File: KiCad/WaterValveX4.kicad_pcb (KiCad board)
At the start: 2 copper layers, 63.2 x 39.1 mm, 51 parts, among them J1 Conn_01x04_Male, J2 Barrel_Jack, J3 Conn_01x03_Male, J4 Conn_01x01_Male, J5 Conn_01x04_Male, J6 Screw_Terminal_01x03, J7 Screw_Terminal_01x03, J8 Screw_Terminal_01x03, J9 Screw_Terminal_01x02, Q1 IRLML2502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

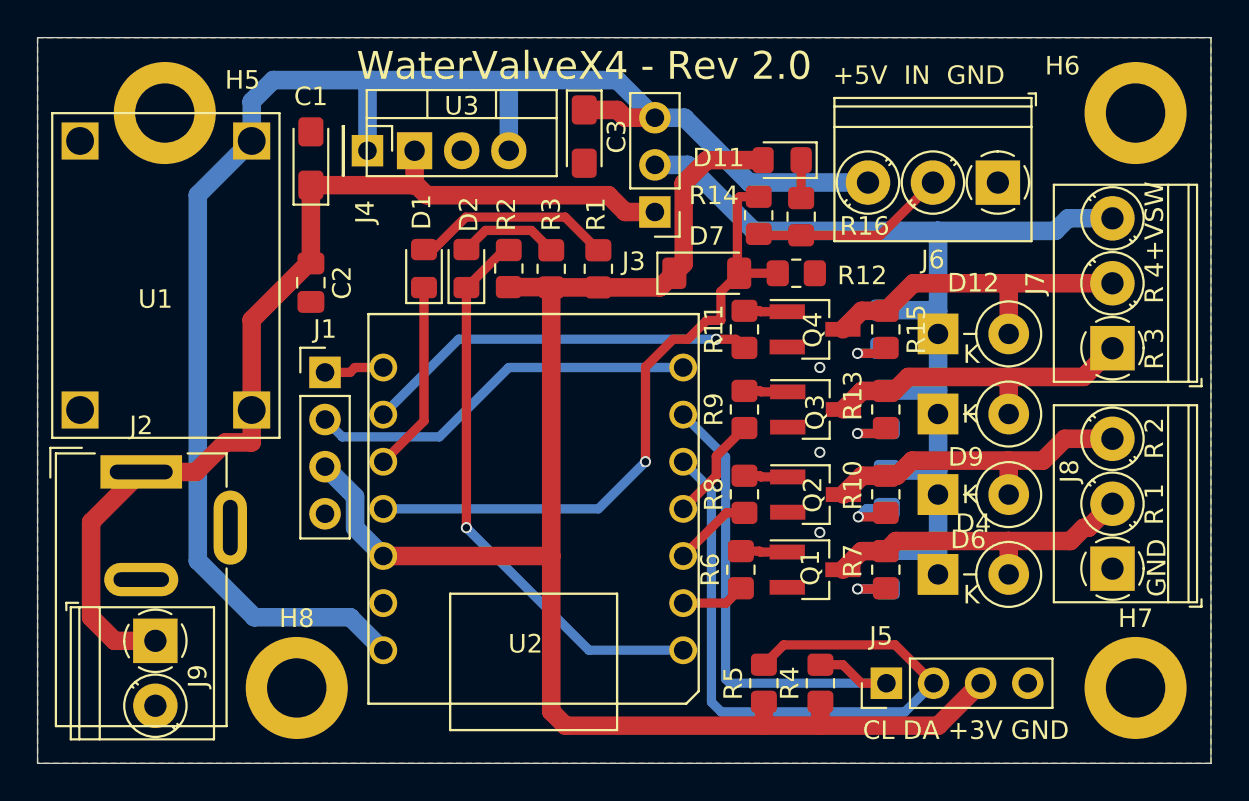
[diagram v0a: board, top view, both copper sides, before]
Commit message: Version 2.0.1 - pulled up / level shifted flow input
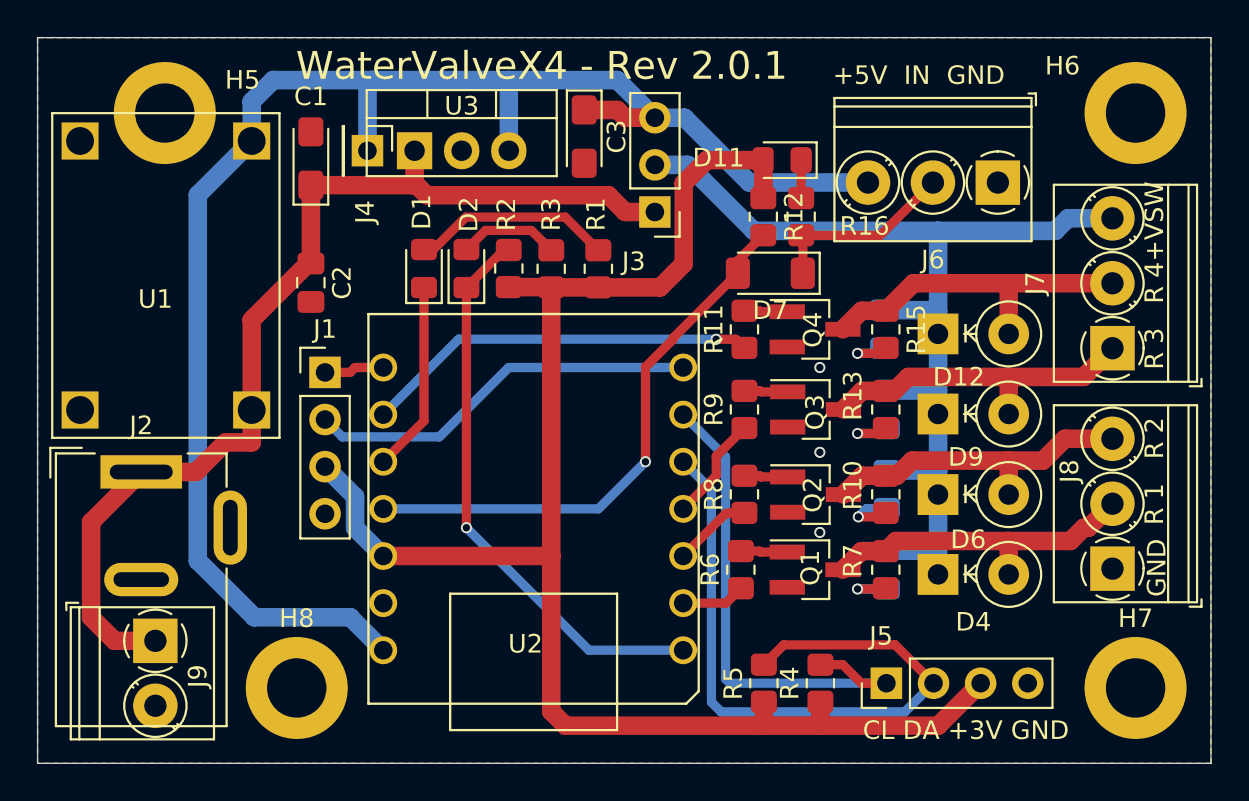
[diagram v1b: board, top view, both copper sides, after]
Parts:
- removed R14: 2.2k, Resistor_SMD:R_0805_2012Metric_Pad1.20x1.40mm_HandSolder
- R10, R13, R15, R7: value 330 -> 1k
- R12: value 3.3k -> 10k
- moved R12 3.53 mm to (175.0, 94.4), turned to -90 degrees
- moved D7 3.43 mm to (175.4, 97.4), turned to 180 degrees
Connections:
- D7 pad 1: +3V3 -> Net-(D7-K)
- J6 pad 2: Net-(J6-Pin_2) -> Net-(D7-K)
- R12 pad 1: /GPIO10 -> +3V3
- R12 pad 2: GND -> /GPIO10
- R16 pad 1: Net-(J6-Pin_2) -> Net-(D7-K)
- R8 pad 1: /GPIO2 -> /GPIO5
- U2 pad 3: /GPIO2 -> /GPIO5
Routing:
- net Net-(J6-Pin_2): track 10.6 -> 0.00 mm
- net Net-(D7-K): track 0.00 -> 10.4 mm
- net /GPIO10: track 35.7 -> 30.0 mm
- net /GPIO5: track 0.00 -> 4.27 mm
- net /GPIO2: track 34.8 -> 30.5 mm
- net +3V3: track 84.1 -> 86.2 mm
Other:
- board text added: "WaterValveX4 - Rev 2.0.1"
- board text removed: "WaterValveX4 - Rev 2.0"
